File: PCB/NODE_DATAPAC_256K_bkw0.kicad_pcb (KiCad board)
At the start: 2 copper layers, 255.3 x 43.2 mm, 32 parts, among them J1 Conn_02x20_Odd_Even, U1 74161, U10 62256, U2 74161, U3 74161, U4 74138, U5 74138, U6 74374, U7 62256, U8 62256, U9 62256

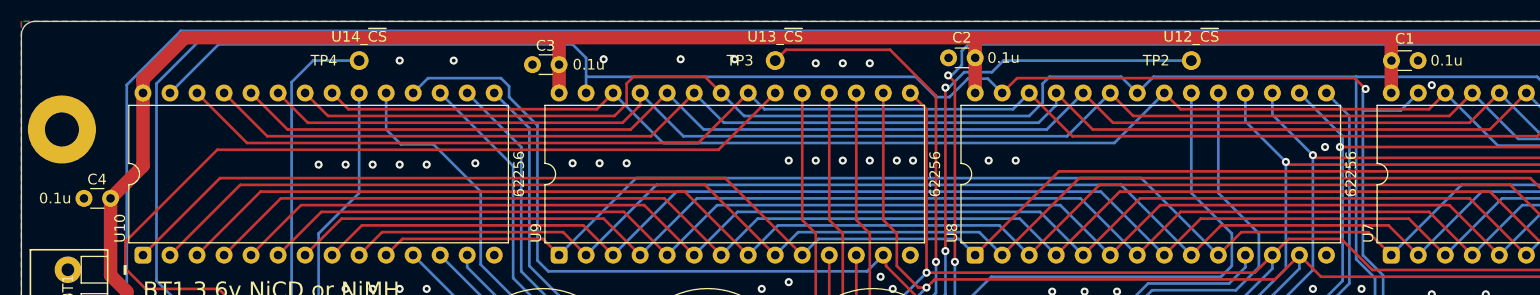
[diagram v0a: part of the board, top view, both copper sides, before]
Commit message: remove unused 3d models
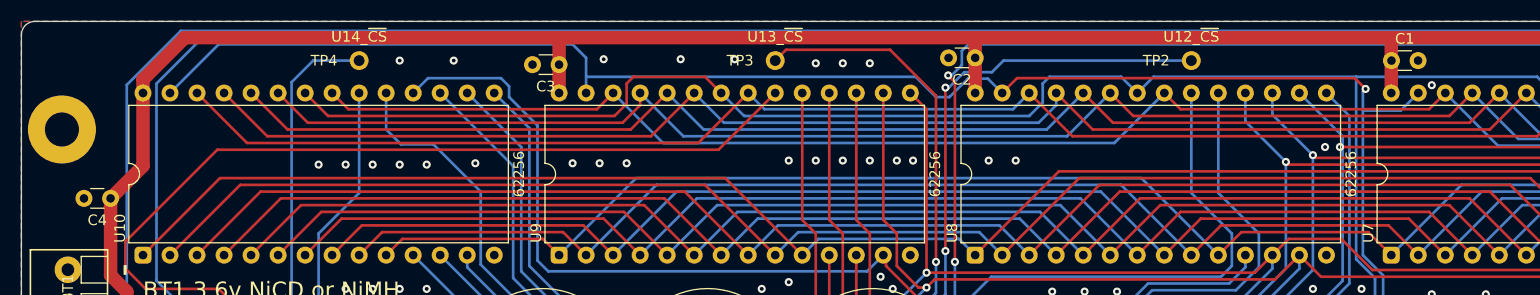
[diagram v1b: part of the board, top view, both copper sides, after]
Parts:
- C1, C2, C3, C4, C5: footprint 000_LOCAL:C_Disc_D3.0mm_W1.6mm_P2.50mm -> 000_LOCAL:C_cer_tht_p2.5
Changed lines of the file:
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@@
     )
   )
-  (footprint "000_LOCAL:C_Disc_D3.0mm_W1.6mm_P2.50mm" (layer "F.Cu")
+  (footprint "000_LOCAL:C_cer_tht_p2.5" (layer "F.Cu")
     (at 27.432 92.837 180)
     (descr "C, Disc series, Radial, pin pitch=2.50mm, , diameter*width=3.0*1.6mm^2, Capacitor, http://www.vishay.com/docs/45233/krseries.pdf")
@@
     (property "ki_keywords" "cap capacitor")
     (attr through_hole)
-    (fp_text reference "C4" (at 1.27 1.778 unlocked) (layer "F.SilkS")
-        (effects (font (size 1 1) (thickness 0.15)))
-    )
-    (fp_text value "0.1u" (at 3.683 0 unlocked) (layer "F.SilkS")
-        (effects (font (size 1 1) (thickness 0.15)) (justify right))
-    )
-    (fp_text user "${REFERENCE}" (at 1.25 0) (layer "F.Fab")
+    (fp_text reference "C4" (at 1.25 -2.05 180) (layer "F.SilkS")
+        (effects (font (size 1 1) (thickness 0.15)))
+    )
+    (fp_text value "0.1u" (at 1.25 2.05 180) (layer "F.Fab")
+        (effects (font (size 1 1) (thickness 0.15)))
+    )
+    (fp_text user "${REFERENCE}" (at 1.25 0 180) (layer "F.Fab")
         (effects (font (size 0.6 0.6) (thickness 0.09)))
     )
@@
     (pad "2" thru_hole circle (at 2.5 0 180) (size 1.6 1.6) (drill 0.8) (layers "*.Cu" "*.Mask")
       (net 1 "GND") (pintype "passive"))
-    (model "${KIPRJMOD}/000_LOCAL.pretty/3dshapes/C_Disc_D3.0mm_W1.6mm_P2.50mm.step"
-      (offset (xyz 0 0 0))
-      (scale (xyz 1 1 1))
-      (rotate (xyz 0 0 0))
+    (model "${KIPRJMOD}/000_LOCAL.pretty/3dshapes/capcer_tht_2.5_decouple.step"
+      (offset (xyz 1.27 0 0))
+      (scale (xyz 1 1 1))
+      (rotate (xyz -90 0 0))
     )
   )
@@
     )
   )
-  (footprint "000_LOCAL:C_Disc_D3.0mm_W1.6mm_P2.50mm" (layer "F.Cu")
+  (footprint "000_LOCAL:C_cer_tht_p2.5" (layer "F.Cu")
     (at 69.596 80.264 180)
     (descr "C, Disc series, Radial, pin pitch=2.50mm, , diameter*width=3.0*1.6mm^2, Capacitor, http://www.vishay.com/docs/45233/krseries.pdf")
@@
     (property "ki_keywords" "cap capacitor")
     (attr through_hole)
-    (fp_text reference "C3" (at 1.27 1.778) (layer "F.SilkS")
-        (effects (font (size 1 1) (thickness 0.15)))
-    )
-    (fp_text value "0.1u" (at -1.27 0 unlocked) (layer "F.SilkS")
-        (effects (font (size 1 1) (thickness 0.15)) (justify left))
-    )
-    (fp_text user "${REFERENCE}" (at 1.25 0) (layer "F.Fab")
+    (fp_text reference "C3" (at 1.25 -2.05 180) (layer "F.SilkS")
+        (effects (font (size 1 1) (thickness 0.15)))
+    )
+    (fp_text value "0.1u" (at 1.25 2.05 180) (layer "F.Fab")
+        (effects (font (size 1 1) (thickness 0.15)))
+    )
+    (fp_text user "${REFERENCE}" (at 1.25 0 180) (layer "F.Fab")
         (effects (font (size 0.6 0.6) (thickness 0.09)))
     )
@@
     (pad "2" thru_hole circle (at 2.5 0 180) (size 1.6 1.6) (drill 0.8) (layers "*.Cu" "*.Mask")
       (net 1 "GND") (pintype "passive"))
-    (model "${KIPRJMOD}/000_LOCAL.pretty/3dshapes/C_Disc_D3.0mm_W1.6mm_P2.50mm.step"
-      (offset (xyz 0 0 0))
-      (scale (xyz 1 1 1))
-      (rotate (xyz 0 0 0))
+    (model "${KIPRJMOD}/000_LOCAL.pretty/3dshapes/capcer_tht_2.5_decouple.step"
+      (offset (xyz 1.27 0 0))
+      (scale (xyz 1 1 1))
+      (rotate (xyz -90 0 0))
     )
   )
@@
       (stroke (width 0.1) (type default)) (layer "F.SilkS"))
   )
-  (footprint "000_LOCAL:C_Disc_D3.0mm_W1.6mm_P2.50mm" (layer "F.Cu")
+  (footprint "000_LOCAL:C_cer_tht_p2.5" (layer "F.Cu")
     (at 236.22 104.648)
     (descr "C, Disc series, Radial, pin pitch=2.50mm, , diameter*width=3.0*1.6mm^2, Capacitor, http://www.vishay.com/docs/45233/krseries.pdf")
@@
     (pad "2" thru_hole circle (at 2.5 0) (size 1.6 1.6) (drill 0.8) (layers "*.Cu" "*.Mask")
       (net 1 "GND") (pintype "passive"))
-    (model "${KIPRJMOD}/000_LOCAL.pretty/3dshapes/C_Disc_D3.0mm_W1.6mm_P2.50mm.step"
-      (offset (xyz 0 0 0))
-      (scale (xyz 1 1 1))
-      (rotate (xyz 0 0 0))
+    (model "${KIPRJMOD}/000_LOCAL.pretty/3dshapes/capcer_tht_2.5_decouple.step"
+      (offset (xyz 1.27 0 0))
+      (scale (xyz 1 1 1))
+      (rotate (xyz -90 0 0))
     )
   )
@@
     )
   )
-  (footprint "000_LOCAL:C_Disc_D3.0mm_W1.6mm_P2.50mm" (layer "F.Cu")
+  (footprint "000_LOCAL:C_cer_tht_p2.5" (layer "F.Cu")
     (at 108.712 79.629 180)
     (descr "C, Disc series, Radial, pin pitch=2.50mm, , diameter*width=3.0*1.6mm^2, Capacitor, http://www.vishay.com/docs/45233/krseries.pdf")
@@
     (property "ki_keywords" "cap capacitor")
     (attr through_hole)
-    (fp_text reference "C2" (at 1.25 1.905) (layer "F.SilkS")
-        (effects (font (size 1 1) (thickness 0.15)))
-    )
-    (fp_text value "0.1u" (at -1.143 0) (layer "F.SilkS")
-        (effects (font (size 1 1) (thickness 0.15)) (justify left))
-    )
-    (fp_text user "${REFERENCE}" (at 1.25 0) (layer "F.Fab")
+    (fp_text reference "C2" (at 1.25 -2.05 180) (layer "F.SilkS")
+        (effects (font (size 1 1) (thickness 0.15)))
+    )
+    (fp_text value "0.1u" (at 1.25 2.05 180) (layer "F.Fab")
+        (effects (font (size 1 1) (thickness 0.15)))
+    )
+    (fp_text user "${REFERENCE}" (at 1.25 0 180) (layer "F.Fab")
         (effects (font (size 0.6 0.6) (thickness 0.09)))
     )
@@
     (pad "2" thru_hole circle (at 2.5 0 180) (size 1.6 1.6) (drill 0.8) (layers "*.Cu" "*.Mask")
       (net 1 "GND") (pintype "passive"))
-    (model "${KIPRJMOD}/000_LOCAL.pretty/3dshapes/C_Disc_D3.0mm_W1.6mm_P2.50mm.step"
-      (offset (xyz 0 0 0))
-      (scale (xyz 1 1 1))
-      (rotate (xyz 0 0 0))
+    (model "${KIPRJMOD}/000_LOCAL.pretty/3dshapes/capcer_tht_2.5_decouple.step"
+      (offset (xyz 1.27 0 0))
+      (scale (xyz 1 1 1))
+      (rotate (xyz -90 0 0))
     )
   )
@@
     )
   )
-  (footprint "000_LOCAL:C_Disc_D3.0mm_W1.6mm_P2.50mm" (layer "F.Cu")
+  (footprint "000_LOCAL:C_cer_tht_p2.5" (layer "F.Cu")
     (at 147.848 79.883)
     (descr "C, Disc series, Radial, pin pitch=2.50mm, , diameter*width=3.0*1.6mm^2, Capacitor, http://www.vishay.com/docs/45233/krseries.pdf")
@@
         (effects (font (size 1 1) (thickness 0.15)))
     )
-    (fp_text value "0.1u" (at 3.663 0 unlocked) (layer "F.SilkS")
-        (effects (font (size 1 1) (thickness 0.15)) (justify left))
+    (fp_text value "0.1u" (at 1.25 2.05) (layer "F.Fab")
+        (effects (font (size 1 1) (thickness 0.15)))
     )
     (fp_text user "${REFERENCE}" (at 1.25 0) (layer "F.Fab")
@@
     (pad "2" thru_hole circle (at 2.5 0) (size 1.6 1.6) (drill 0.8) (layers "*.Cu" "*.Mask")
       (net 1 "GND") (pintype "passive"))
-    (model "${KIPRJMOD}/000_LOCAL.pretty/3dshapes/C_Disc_D3.0mm_W1.6mm_P2.50mm.step"
-      (offset (xyz 0 0 0))
-      (scale (xyz 1 1 1))
-      (rotate (xyz 0 0 0))
-    )
-  )
+    (model "${KIPRJMOD}/000_LOCAL.pretty/3dshapes/capcer_tht_2.5_decouple.step"
+      (offset (xyz 1.27 0 0))
+      (scale (xyz 1 1 1))
+      (rotate (xyz -90 0 0))
+    )
+  )

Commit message: readme, software, remove nimh from new board
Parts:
- removed the BT1 at (23.4, 103.0)
- removed BT1_PACK: FL3V80H, 000_LOCAL:FL3V80H
- removed R1: 200, 000_LOCAL:R_Axial_DIN0207_L6.3mm_D2.5mm_P10.16mm_Horizontal
- moved BT1 2.99 mm to (256.5, 91.2), turned to 90 degrees
- turned D3 to 0 degrees
- renumbered BT2 to BT1
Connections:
- BT1 pad 1: Net-(BT2-+) -> /BATT+
- D3 pad 2: Net-(BT2-+) -> /BATT+
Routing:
- net Net-(BT2-+): track 21.0 -> 0.00 mm
- net /BATT+: track 16.3 -> 6.35 mm
- net VMEM: track 270.5 -> 267.8 mm
- net GND: vias 87 -> 88
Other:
- board text added: "CR2032"
- board text removed: "+"
- board text removed: "-"
- board text removed: "BT1 3.6v NiCD or NiMH"
- board text removed: "BT2 3v CR2032"
- board text removed: "Use only one BT1 or BT2"

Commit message: truth table
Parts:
- added C6: 0.1u, 000_LOCAL:C_cer_tht_p2.5, F.Cu at (237.9, 117.2)
- added C7: 0.1u, 000_LOCAL:C_cer_tht_p2.5, F.Cu at (236.2, 96.0)
- moved C5 30.8 mm to (207.0, 114.6)
- renumbered D3 to D2, D2 to D3, U3 to U1, U1 to U3
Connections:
- net /_RAM_RST renamed /SLEEP
- net Net-(U1-CEP) renamed /TC1
- net Net-(U10-A11) renamed /A7
- net Net-(U10-A12) renamed /A2
- net Net-(U10-A14) renamed /A1
- net Net-(U10-A5) renamed /A4
- net Net-(U10-A6) renamed /A3
- net Net-(U10-A7) renamed /A0
- net Net-(U10-A8) renamed /A5
- net Net-(U10-A9) renamed /A6
- net Net-(U2-CEP) renamed /TC0
- net Net-(U5-A1) renamed /A16
- net Net-(U5-A2) renamed /A17
- J1 pad 13: /A8 -> /BUS_A8
- J1 pad 14: /A9 -> /BUS_A9
- J1 pad 15: /A10 -> unconnected-(J1-Pin_15-Pad15)
- J1 pad 16: /A11 -> unconnected-(J1-Pin_16-Pad16)
- J1 pad 17: /A12 -> unconnected-(J1-Pin_17-Pad17)
- J1 pad 18: /A13 -> unconnected-(J1-Pin_18-Pad18)
- J1 pad 19: /A14 -> unconnected-(J1-Pin_19-Pad19)
- J1 pad 20: /A15 -> unconnected-(J1-Pin_20-Pad20)
- J1 pad 25: /IO/~{M} -> unconnected-(J1-Pin_25-Pad25)
- J1 pad 26: /S0 -> unconnected-(J1-Pin_26-Pad26)
- J1 pad 27: /~{ALE} -> unconnected-(J1-Pin_27-Pad27)
- J1 pad 28: /S1 -> unconnected-(J1-Pin_28-Pad28)
- J1 pad 29: /CLK -> unconnected-(J1-Pin_29-Pad29)
- J1 pad 32: /~{RESET} -> unconnected-(J1-Pin_32-Pad32)
- J1 pad 33: /INTR -> unconnected-(J1-Pin_33-Pad33)
- J1 pad 34: /INTA -> unconnected-(J1-Pin_34-Pad34)
- U1 pad 11: Net-(U10-A10) -> /A8
- U10 pad 10: Net-(U1-Q1) -> /A14
- U10 pad 21: Net-(U10-A10) -> /A8
- U10 pad 26: Net-(U1-Q0) -> /A13
- U10 pad 6: Net-(U10-A4) -> /A12
- U10 pad 7: Net-(U10-A3) -> /A11
- U10 pad 8: Net-(U10-A2) -> /A10
- U10 pad 9: Net-(U10-A1) -> /A9
- U2 pad 11: Net-(U10-A4) -> /A12
- U2 pad 12: Net-(U10-A3) -> /A11
- U2 pad 13: Net-(U10-A2) -> /A10
- U2 pad 14: Net-(U10-A1) -> /A9
- U3 pad 13: Net-(U1-Q1) -> /A14
- U3 pad 14: Net-(U1-Q0) -> /A13
- U4 pad 1: /A8 -> /BUS_A8
- U4 pad 2: /A9 -> /BUS_A9
- U5 pad 1: Net-(U5-A0) -> /A15
- U6 pad 5: Net-(U5-A0) -> /A15
- U7 pad 1: Net-(U1-Q1) -> /A14
- U7 pad 2: Net-(U10-A1) -> /A9
- U7 pad 21: Net-(U1-Q0) -> /A13
- U7 pad 26: Net-(U10-A10) -> /A8
- U7 pad 3: Net-(U10-A2) -> /A10
- U7 pad 4: Net-(U10-A3) -> /A11
- U7 pad 5: Net-(U10-A4) -> /A12
- U8 pad 10: Net-(U1-Q1) -> /A14
- U8 pad 21: Net-(U10-A10) -> /A8
- U8 pad 26: Net-(U1-Q0) -> /A13
- U8 pad 6: Net-(U10-A4) -> /A12
- U8 pad 7: Net-(U10-A3) -> /A11
- U8 pad 8: Net-(U10-A2) -> /A10
- U8 pad 9: Net-(U10-A1) -> /A9
- U9 pad 1: Net-(U1-Q1) -> /A14
- U9 pad 2: Net-(U10-A1) -> /A9
- U9 pad 21: Net-(U1-Q0) -> /A13
- U9 pad 26: Net-(U10-A10) -> /A8
- U9 pad 3: Net-(U10-A2) -> /A10
- U9 pad 4: Net-(U10-A3) -> /A11
- U9 pad 5: Net-(U10-A4) -> /A12
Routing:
- net Net-(U1-Q0): track 259.5 -> 0.00 mm
- net /A13: track 0.00 -> 259.5 mm
- net Net-(U1-Q1): track 240.3 -> 0.00 mm
- net /A14: track 0.00 -> 240.3 mm
- net Net-(U10-A1): track 192.7 -> 0.00 mm
- net Net-(U10-A4): track 192.7 -> 0.00 mm
- net Net-(U10-A3): track 192.7 -> 0.00 mm
- net Net-(U10-A2): track 192.7 -> 0.00 mm
- net /A12: track 0.00 -> 192.7 mm
- net /A11: track 0.00 -> 192.7 mm
- net /A10: track 0.00 -> 192.7 mm
- net Net-(U10-A10): track 180.6 -> 0.00 mm
- net Net-(U5-A0): track 167.4 -> 0.00 mm, vias 1 -> 0
- net /A15: track 0.00 -> 167.4 mm, vias 0 -> 1
- net /BUS_A8: track 0.00 -> 106.7 mm, vias 0 -> 1
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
